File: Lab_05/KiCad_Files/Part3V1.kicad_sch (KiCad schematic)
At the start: 29 parts, among them Q1 NPN, Q2 PNP, Q3 NPN, Q4 NPN, Q5 NPN, Q6 NPN, Q7 NPN, Q8 NPN, Q9 PNP

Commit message: Continue Lab 5
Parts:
- removed I1, I2: IREF1, symbol Simulation_SPICE:IDC
- removed LA1: Lamp, symbol Device:Lamp
- added C3: 0.1uF, symbol Device:C
- added LA301: ${SIM.PARAMS}, symbol Device:Lamp
- added R10 (x2): 10K, symbol Device:R
- C2, C3: value C -> 6800pF
- R10, R11, R14, R15, R2, R3, R4, R7: value R -> 1K
- R12, R5: value 1000R -> 1M
- R13, R6: value R -> 2K2
- R8: value R -> 100
- R9: value 2000R -> 150K
- V1: value VSIN -> VSIN_P3A
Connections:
- net -15V is gone; now on net GND: R15.2, R2.2, R8.2
- net +15V: now also R10.1, R10.1
- net GND: now also LA301.1 (-)
- net at Q2.1 (C), Q9.1 (C): now also LA301.2 (+)
- net at Q6.2 (B), R12.1: now also R10.2
- net at Q3.2 (B): now also R10.2
- net at V1.1: now also C3.1; no longer Q5.2 (B)
- new net: C3.2, Q5.2 (B)
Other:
- company: (none) -> Jim Horwitz & Mark Vaughn, Jork Incorporated
- moved on the sheet: C2, C3, Q1, Q2, Q3, Q4, Q5, Q6, Q7, Q8, Q9, R10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

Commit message: Finish Saturday Schematics
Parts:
- removed C3: 0.1uF, symbol Device:C
- R8: value 100 -> 68R
- R9: value 150K -> 6K8
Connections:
- net at V1.1: now also Q5.2 (B)
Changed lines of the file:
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@@
-    (stroke (width 0) (type default))
-  )
-  (wire (pts (xy 46.99 104.14) (xy 49.53 104.14))
     (stroke (width 0) (type default))
   )
@@
     (stroke (width 0) (type default))
   )
-  (wire (pts (xy 57.15 104.14) (xy 72.39 104.14))
+  (wire (pts (xy 46.99 104.14) (xy 72.39 104.14))
     (stroke (width 0) (type default))
   )
@@
       (effects (font (size 1.27 1.27)) (justify left))
     )
-    (property "Value" "150K" (at 82.55 95.25 0)
+    (property "Value" "6K8" (at 82.55 95.25 0)
       (effects (font (size 1.27 1.27)) (justify left))
     )
@@
         )
         (path "/9fa84b6a-7d78-4b93-9106-2eb97c609eaa/92df8f0c-b3ae-4e10-833d-91d59ac40b8d"
-          (reference "C303") (unit 1)
+          (reference "C302") (unit 1)
         )
         (path "/9fa84b6a-7d78-4b93-9106-2eb97c609eaa/3dc750a5-52be-410a-8665-921cbeb63b7d"
@@
         )
         (path "/9fa84b6a-7d78-4b93-9106-2eb97c609eaa/92df8f0c-b3ae-4e10-833d-91d59ac40b8d"
-          (reference "C302") (unit 1)
+          (reference "C301") (unit 1)
         )
         (path "/9fa84b6a-7d78-4b93-9106-2eb97c609eaa/3dc750a5-52be-410a-8665-921cbeb63b7d"
@@
     )
   )
-  (symbol (lib_id "Device:C") (at 53.34 104.14 90) (unit 1)
-    (in_bom yes) (on_board yes) (dnp no)
-    (property "Reference" "C3" (at 53.34 97.79 90)
-      (effects (font (size 1.27 1.27)))
-    )
-    (property "Value" "0.1uF" (at 53.34 100.33 90)
-      (effects (font (size 1.27 1.27)))
-    )
-    (property "Footprint" "" (at 57.15 103.1748 0)
-      (effects (font (size 1.27 1.27)) hide)
-    )
-    (property "Datasheet" "~" (at 53.34 104.14 0)
-      (effects (font (size 1.27 1.27)) hide)
-    )
-    (pin "1")
-    (pin "2")
-    (instances
-      (project "Lab05"
-        (path "/9fa84b6a-7d78-4b93-9106-2eb97c609eaa"
-          (reference "C3") (unit 1)
-        )
-        (path "/9fa84b6a-7d78-4b93-9106-2eb97c609eaa/92df8f0c-b3ae-4e10-833d-91d59ac40b8d"
-          (reference "C301") (unit 1)
-        )
-        (path "/9fa84b6a-7d78-4b93-9106-2eb97c609eaa/3dc750a5-52be-410a-8665-921cbeb63b7d"
-          (reference "C4") (unit 1)
-        )
-        (path "/9fa84b6a-7d78-4b93-9106-2eb97c609eaa/a137afc5-afed-494e-bb1a-b2a03cb8cb70"
-          (reference "C4") (unit 1)
-        )
-      )
-    )
-  )
   (symbol (lib_id "Simulation_SPICE:NPN") (at 165.1 62.23 0) (unit 1)
     (in_bom yes) (on_board yes) (dnp no) (fields_autoplaced)
@@
       (effects (font (size 1.27 1.27)) (justify left))
     )
-    (property "Value" "100" (at 82.55 115.57 0)
-      (effects (font (size 1.27 1.27)) (justify left))
-    )
+    (property "Value" "68R" (at 82.55 115.57 0)
+      (effects (font (size 1.27 1.27)) (justify left))
+    )

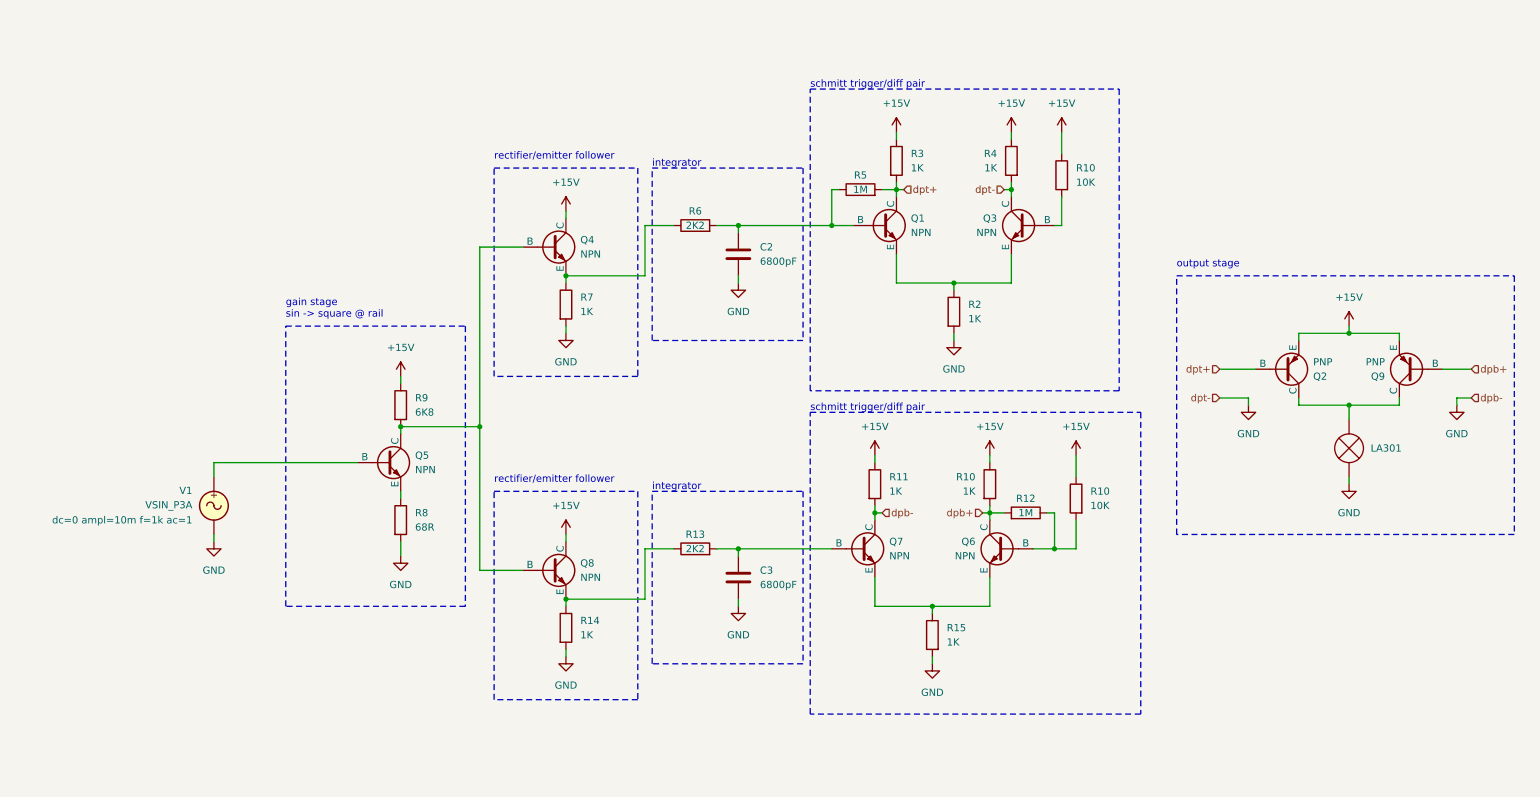
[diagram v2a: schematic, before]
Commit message: Revise part 3 Version 1
For next revision:
- add collector resistor to Q304
- remove R309
- add emitter follower after integrator
For the future:
- add more poles to bandpass!!
- maybe a resonant filter?
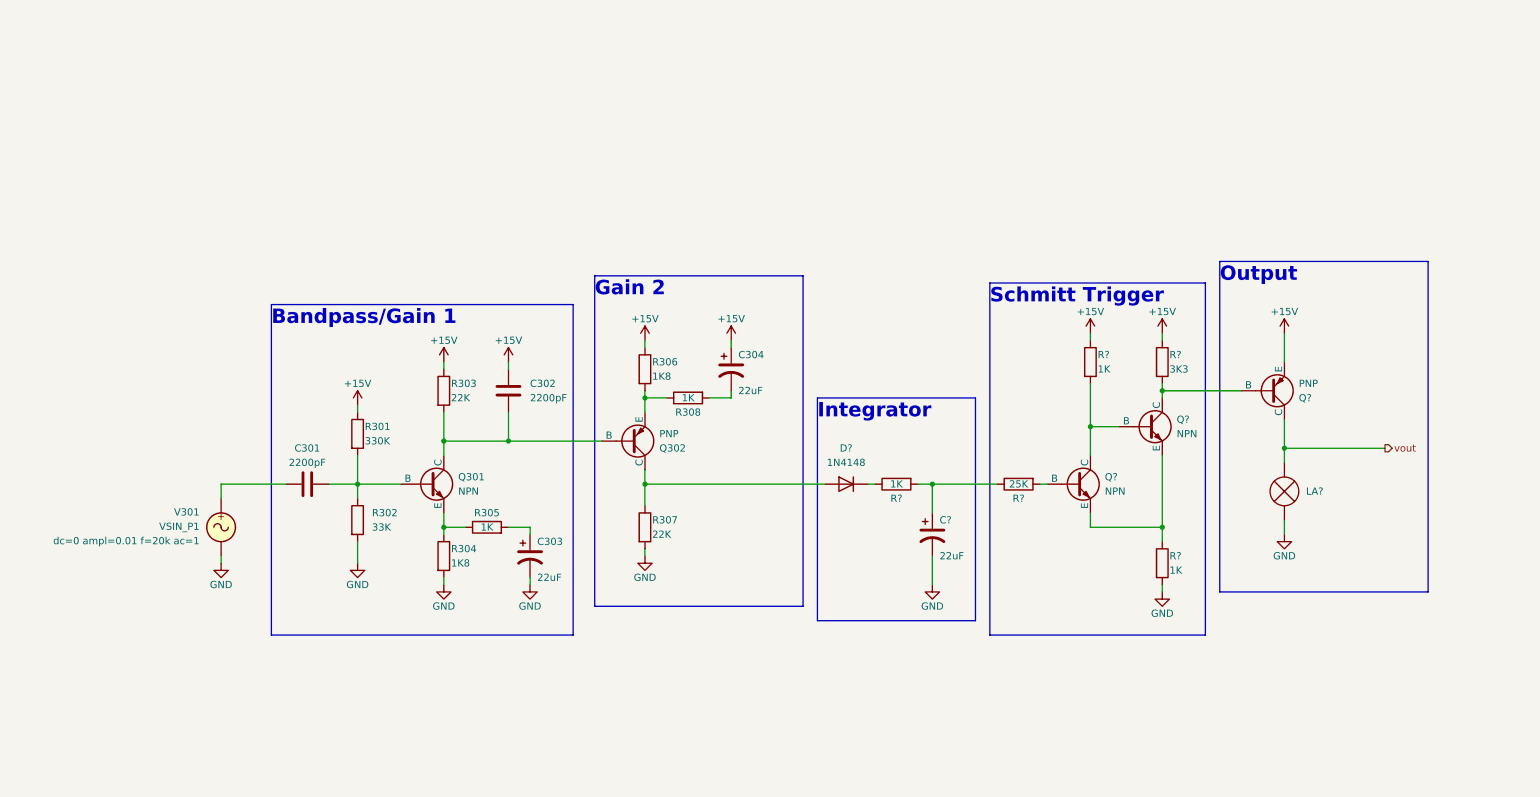
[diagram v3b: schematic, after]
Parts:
- removed C2, C3: 6800pF, symbol Device:C
- removed LA301: ${SIM.PARAMS}, symbol Device:Lamp
- removed Q1, Q3, Q4, Q5, Q6, Q7, Q8: NPN, symbol Simulation_SPICE:NPN
- removed Q2, Q9: PNP, symbol Simulation_SPICE:PNP
- removed R10 (x2): 10K, symbol Device:R
- removed R10, R11, R14, R15, R2, R3, R4, R7: 1K, symbol Device:R
- removed R12, R5: 1M, symbol Device:R
- removed R13, R6: 2K2, symbol Device:R
- removed R8: 68R, symbol Device:R
- removed R9: 6K8, symbol Device:R
- removed V1: VSIN_P3A, symbol Simulation_SPICE:VSIN
- added C301, C302: 2200pF, symbol Device:C
- added C303, C304, C?: 22uF, symbol Device:C_Polarized_US
- added D?: 1N4148, Diode_THT:D_DO-35_SOD27_P7.62mm_Horizontal, symbol Diode:1N4148
- added LA?: ${SIM.PARAMS}, symbol Device:Lamp
- added Q301, Q? (x2): NPN, symbol Simulation_SPICE:NPN
- added Q302, Q?: PNP, symbol Simulation_SPICE:PNP
- added R301: 330K, symbol Device:R
- added R302: 33K, symbol Device:R
- added R303, R307: 22K, symbol Device:R
- added R304, R306: 1K8, symbol Device:R
- added R305, R308, R? (x3): 1K, symbol Device:R
- added R?: 25K, symbol Device:R
- added R?: 3K3, symbol Device:R
- added V301: VSIN_P1, symbol Simulation_SPICE:VSIN
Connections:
- net +15V: now also C302.1, C304.1, Q?.3 (E), R301.1, R303.1, R306.1, R?.1, R?.1
- net GND: now also C303.2, C?.2, LA?.1 (-), R302.2, R304.2, R307.2, R?.2, V301.2
- new net: C301.1, V301.1
- new net: D?.1 (K), R?.1
- new net: C?.1, R?.1, R?.2
- new net: Q301.3 (E), R304.1, R305.1
- new net: Q?.2 (B), R?.2
- new net: C301.2, Q301.2 (B), R301.2, R302.1
- new net: Q302.3 (E), R306.2, R308.1
- new net: C304.2, R308.2
- new net: Q?.1 (C), Q?.2 (B), R?.2 (x2)
- new net: C302.2, Q301.1 (C), Q302.2 (B), R303.2
- new net: D?.2 (A), Q302.1 (C), R307.1
- new net: C303.1, R305.2
- new net: Q?.3 (E), Q?.3 (E), R?.1
- new net vout: LA?.2 (+), Q?.1 (C)
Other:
- note added: "Bandpass/Gain 1"
- note added: "Gain 2"
- note added: "Integrator"
- note added: "Output"
- note added: "Schmitt Trigger"
- note removed: "gain stage sin -> square @ rail"
- note removed: "integrator"
- note removed: "output stage"
- note removed: "rectifier/emitter follower"
- note removed: "schmitt trigger/diff pair"

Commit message: Annotate Part 3
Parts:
- gave numbers to parts that had none: 11
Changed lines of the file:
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@@
   (symbol (lib_id "power:+15V") (at 236.22 81.28 0) (unit 1)
     (in_bom yes) (on_board yes) (dnp no)
-    (property "Reference" "#PWR0316" (at 236.22 85.09 0)
+    (property "Reference" "#PWR0315" (at 236.22 85.09 0)
       (effects (font (size 1.27 1.27)) hide)
     )
@@
       (project "Lab05"
         (path "/9fa84b6a-7d78-4b93-9106-2eb97c609eaa/92df8f0c-b3ae-4e10-833d-91d59ac40b8d"
-          (reference "#PWR0316") (unit 1)
+          (reference "#PWR0315") (unit 1)
         )
       )
@@
   (symbol (lib_id "Device:R") (at 167.64 107.95 90) (mirror x) (unit 1)
     (in_bom yes) (on_board yes) (dnp no)
-    (property "Reference" "R?" (at 167.64 110.49 90)
+    (property "Reference" "R309" (at 167.64 110.49 90)
       (effects (font (size 1.27 1.27)))
     )
@@
       (project "Lab05"
         (path "/9fa84b6a-7d78-4b93-9106-2eb97c609eaa/92df8f0c-b3ae-4e10-833d-91d59ac40b8d"
-          (reference "R?") (unit 1)
+          (reference "R309") (unit 1)
         )
       )
@@
   (symbol (lib_id "Device:R") (at 189.23 107.95 90) (mirror x) (unit 1)
     (in_bom yes) (on_board yes) (dnp no)
-    (property "Reference" "R?" (at 189.23 110.49 90)
+    (property "Reference" "R310" (at 189.23 110.49 90)
       (effects (font (size 1.27 1.27)))
     )
@@
       (project "Lab05"
         (path "/9fa84b6a-7d78-4b93-9106-2eb97c609eaa/92df8f0c-b3ae-4e10-833d-91d59ac40b8d"
-          (reference "R?") (unit 1)
+          (reference "R310") (unit 1)
         )
       )
@@
   (symbol (lib_id "Device:R") (at 201.93 86.36 0) (unit 1)
     (in_bom yes) (on_board yes) (dnp no)
-    (property "Reference" "R?" (at 203.2 85.09 0)
+    (property "Reference" "R311" (at 203.2 85.09 0)
       (effects (font (size 1.27 1.27)) (justify left))
     )
@@
       (project "Lab05"
         (path "/9fa84b6a-7d78-4b93-9106-2eb97c609eaa/92df8f0c-b3ae-4e10-833d-91d59ac40b8d"
-          (reference "R?") (unit 1)
+          (reference "R311") (unit 1)
         )
       )
@@
   (symbol (lib_id "Device:R") (at 214.63 86.36 0) (unit 1)
     (in_bom yes) (on_board yes) (dnp no)
-    (property "Reference" "R?" (at 215.9 85.09 0)
+    (property "Reference" "R312" (at 215.9 85.09 0)
       (effects (font (size 1.27 1.27)) (justify left))
     )
@@
       (project "Lab05"
         (path "/9fa84b6a-7d78-4b93-9106-2eb97c609eaa/92df8f0c-b3ae-4e10-833d-91d59ac40b8d"
-          (reference "R?") (unit 1)
+          (reference "R312") (unit 1)
         )
       )
@@
   (symbol (lib_id "Device:Lamp") (at 236.22 109.22 0) (unit 1)
     (in_bom yes) (on_board yes) (dnp no) (fields_autoplaced)
-    (property "Reference" "LA?" (at 240.03 109.22 0)
+    (property "Reference" "LA301" (at 240.03 109.22 0)
       (effects (font (size 1.27 1.27)) (justify left))
     )
@@
       (project "Lab05"
         (path "/9fa84b6a-7d78-4b93-9106-2eb97c609eaa/92df8f0c-b3ae-4e10-833d-91d59ac40b8d"
-          (reference "LA?") (unit 1)
+          (reference "LA301") (unit 1)
         )
       )
@@
   (symbol (lib_id "Device:C_Polarized_US") (at 173.99 116.84 0) (unit 1)
     (in_bom yes) (on_board yes) (dnp no)
-    (property "Reference" "C?" (at 175.26 114.3 0)
+    (property "Reference" "C305" (at 175.26 114.3 0)
       (effects (font (size 1.27 1.27)) (justify left))
     )
@@
       (project "Lab05"
         (path "/9fa84b6a-7d78-4b93-9106-2eb97c609eaa/92df8f0c-b3ae-4e10-833d-91d59ac40b8d"
-          (reference "C?") (unit 1)
+          (reference "C305") (unit 1)
         )
       )
@@
   (symbol (lib_id "Simulation_SPICE:NPN") (at 199.39 107.95 0) (unit 1)
     (in_bom yes) (on_board yes) (dnp no) (fields_autoplaced)
-    (property "Reference" "Q?" (at 204.47 106.68 0)
+    (property "Reference" "Q303" (at 204.47 106.68 0)
       (effects (font (size 1.27 1.27)) (justify left))
     )
@@
       (project "Lab05"
         (path "/9fa84b6a-7d78-4b93-9106-2eb97c609eaa/92df8f0c-b3ae-4e10-833d-91d59ac40b8d"
-          (reference "Q?") (unit 1)
+          (reference "Q303") (unit 1)
         )
       )
@@
   (symbol (lib_id "Diode:1N4148") (at 158.75 107.95 0) (mirror y) (unit 1)
     (in_bom yes) (on_board yes) (dnp no) (fields_autoplaced)
-    (property "Reference" "D?" (at 158.75 101.6 0)
+    (property "Reference" "D301" (at 158.75 101.6 0)
       (effects (font (size 1.27 1.27)))
     )
@@
       (project "Lab05"
         (path "/9fa84b6a-7d78-4b93-9106-2eb97c609eaa/92df8f0c-b3ae-4e10-833d-91d59ac40b8d"
-          (reference "D?") (unit 1)
+          (reference "D301") (unit 1)
         )
       )
@@
   (symbol (lib_id "Simulation_SPICE:PNP") (at 233.68 91.44 0) (mirror x) (unit 1)
     (in_bom yes) (on_board yes) (dnp no)
-    (property "Reference" "Q?" (at 238.76 92.71 0)
+    (property "Reference" "Q305" (at 238.76 92.71 0)
       (effects (font (size 1.27 1.27)) (justify left))
     )
@@
       (project "Lab05"
         (path "/9fa84b6a-7d78-4b93-9106-2eb97c609eaa/92df8f0c-b3ae-4e10-833d-91d59ac40b8d"
-          (reference "Q?") (unit 1)
+          (reference "Q305") (unit 1)
         )
       )
@@
   (symbol (lib_id "Simulation_SPICE:NPN") (at 212.09 97.79 0) (unit 1)
     (in_bom yes) (on_board yes) (dnp no) (fields_autoplaced)
-    (property "Reference" "Q?" (at 217.17 96.52 0)
+    (property "Reference" "Q304" (at 217.17 96.52 0)
       (effects (font (size 1.27 1.27)) (justify left))
     )
@@
       (project "Lab05"
         (path "/9fa84b6a-7d78-4b93-9106-2eb97c609eaa/92df8f0c-b3ae-4e10-833d-91d59ac40b8d"
-          (reference "Q?") (unit 1)
+          (reference "Q304") (unit 1)
         )
       )
@@
   (symbol (lib_id "power:GND") (at 236.22 116.84 0) (unit 1)
     (in_bom yes) (on_board yes) (dnp no)
-    (property "Reference" "#PWR0315" (at 236.22 123.19 0)
+    (property "Reference" "#PWR0316" (at 236.22 123.19 0)
       (effects (font (size 1.27 1.27)) hide)
     )
@@
       (project "Lab05"
         (path "/9fa84b6a-7d78-4b93-9106-2eb97c609eaa/92df8f0c-b3ae-4e10-833d-91d59ac40b8d"
-          (reference "#PWR0315") (unit 1)
+          (reference "#PWR0316") (unit 1)
         )
       )
@@
   (symbol (lib_id "Device:R") (at 214.63 121.92 0) (unit 1)
     (in_bom yes) (on_board yes) (dnp no)
-    (property "Reference" "R?" (at 215.9 120.65 0)
+    (property "Reference" "R313" (at 215.9 120.65 0)
       (effects (font (size 1.27 1.27)) (justify left))
     )
@@
       (project "Lab05"
         (path "/9fa84b6a-7d78-4b93-9106-2eb97c609eaa/92df8f0c-b3ae-4e10-833d-91d59ac40b8d"
-          (reference "R?") (unit 1)
-        )
-      )
+          (reference "R313") (unit 1)
+        )
+      )

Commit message: Finish Lab 5
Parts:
- removed C304: 22uF, symbol Device:C_Polarized_US
- removed Q302: PNP, symbol Simulation_SPICE:PNP
- removed R306: 1K8, symbol Device:R
- removed R307: 22K, symbol Device:R
- removed R308, R309: 1K, symbol Device:R
- added C?: 22uF, symbol Device:C_Polarized_US
- added C? (x2): 2200pF, symbol Device:C
- added Q? (x4): NPN, symbol Simulation_SPICE:NPN
- added R?: 1K8, symbol Device:R
- added R? (x4): 1K, symbol Device:R
- added R?: 22K, symbol Device:R
- added R?: 33K, symbol Device:R
- added R?: 1M, symbol Device:R
- added R?: 100R, symbol Device:R
- added R?: 330K, symbol Device:R
- R310: value 25K -> 560K
- R311: value 1K -> 3K3
- R312: value 3K3 -> 1K
- R313: value 1K -> 10R
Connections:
- net GND: now also C?.2, R?.2, R?.2, R?.2, R?.2, R?.2, R?.2
- net at D301.1 (K): now also C305.1, Q?.2 (B), R?.1
- net at R310.1: now also Q?.3 (E), R?.1; no longer C305.1
- net at C302.2, Q301.1 (C), R303.2: now also Q?.2 (B)
- net at Q304.1 (C), R312.2: now also R?.1; no longer Q305.2 (B)
- net PK_In: now reaches D301.2 (A)
- net PK_In: now also Q?.3 (E), R?.1
- net +15V renamed VCC
- net VCC: now also C?.1, Q?.1 (C), Q?.1 (C), Q?.1 (C), R?.1, R?.1
- new net: C?.1, R?.2
- new net: C?.1, Q?.3 (E), R?.1
- new net: C?.2, Q?.2 (B), R?.1, R?.2
- new net: Q?.3 (E), R?.1, R?.1
- new net: C?.2, Q?.1 (C), Q?.2 (B), R?.2
- new net: Q305.2 (B), R?.2
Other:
- note added: "Bandpass/Gain 2"
- note added: "PK Detector"
- note removed: "Gain 2"
- note removed: "Integrator"
- moved on the sheet: C301, C302, C303, C305, D301, LA301, Q301, Q303, Q304, Q305, R301, R302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
